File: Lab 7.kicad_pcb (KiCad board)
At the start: 2 copper layers, 75 x 75 mm, 45 parts, among them IC1 TPS2832D, Q1 CSD18534KCS, Q2 CSD18534KCS, U1 TLV2372

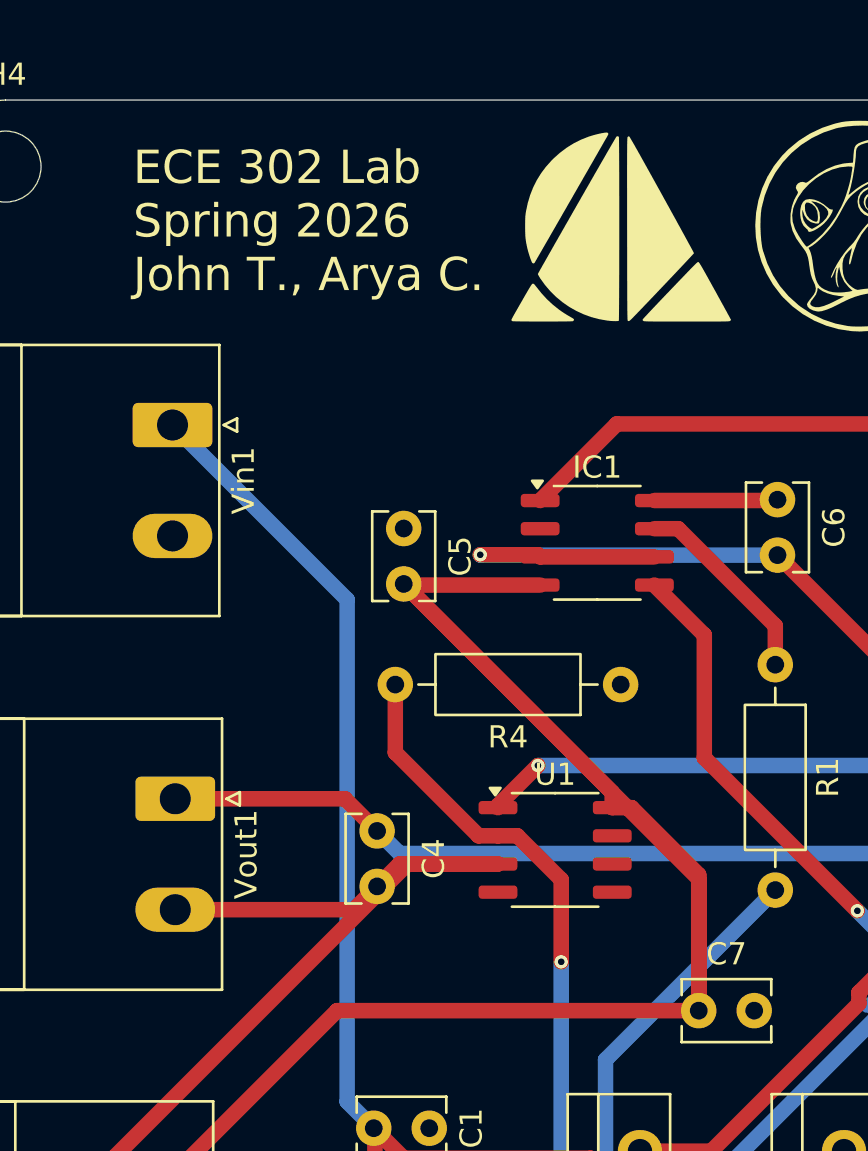
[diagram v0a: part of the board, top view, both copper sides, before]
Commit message: connecting ground
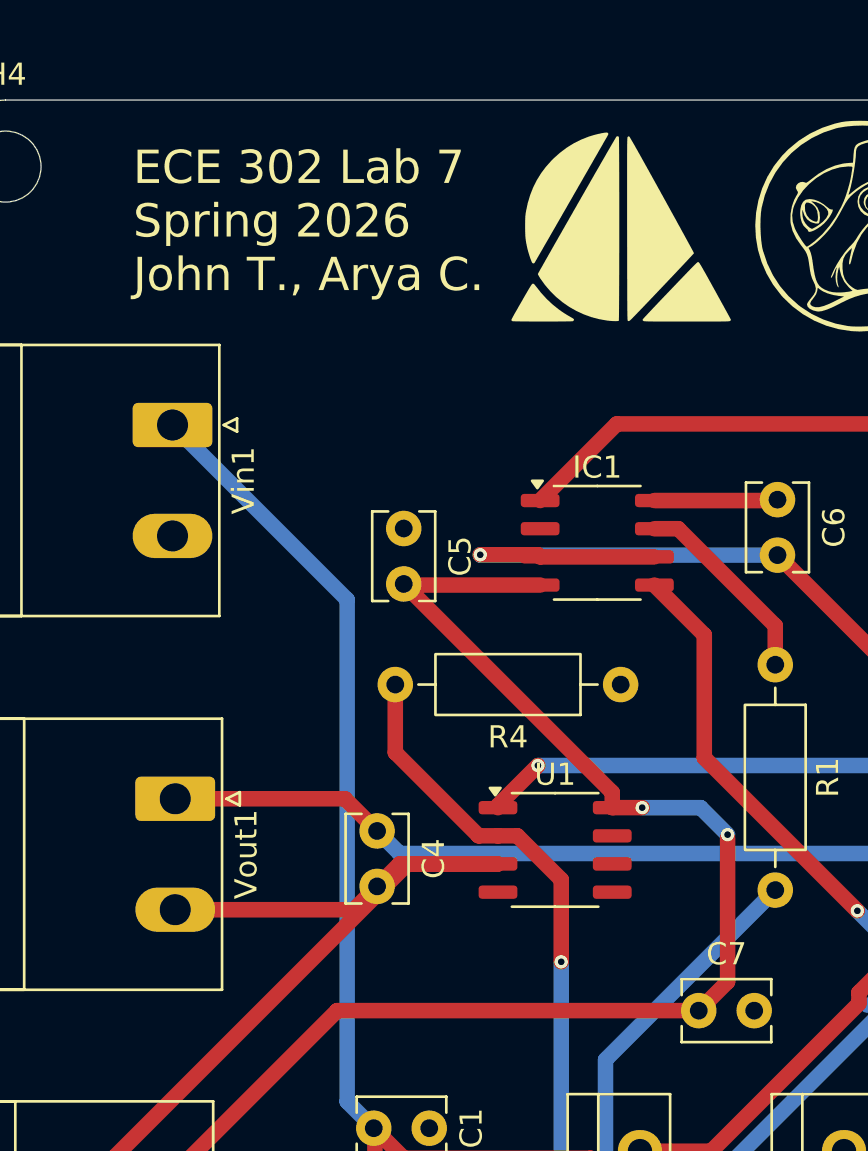
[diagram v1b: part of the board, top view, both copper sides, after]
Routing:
- net 10V: track 101.7 -> 79.9 mm, vias 0 -> 2
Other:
- board text added: "ECE 302 Lab 7 Spring 2026 John T., Arya C."
- board text removed: "ECE 302 Lab Spring 2026 John T., Arya C."
